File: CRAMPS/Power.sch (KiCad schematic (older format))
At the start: 19 parts, among them P101 HB_IN, P103 PS-ON, P105 12V-AUX, P107 MOT_IN, P108 POWER_IN, P219 EXT_5V, U3 LM7812

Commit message: Work in progress, many schematic updates, added PCB files
Signed-off-by: Charles Steinkuehler <charles@steinkuehler.net>
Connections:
- net labels added: D3.3V, SYS_5V, VDD_5V
- net labels removed: DUE_5V, FD_5V, IOREF
- wire segments 67 -> 83
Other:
- note added: "BeagleBone Logic supply is always 3.3V"
- note added: "SYS_5V: Low-current supply\nVDD_5V: DC Input Jack"
- note removed: "Note: On R3 compatible Arduinos, IOREF \nwill supply 3.3V (Due), or 5V (Mega).\n\nIf IOREF is not provided (non-R3) then it \nmust be a 5V Arduino so set VSEL to 5V."
- note removed: "VSEL - Select logic voltage\n1-2 = Autoselect by IOREF\n2-3 = 5V"
- moved on the sheet: JP101, JP201, P219

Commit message: Schematic updates mostly complete Pending pin assignment which will happen based on PCB layout Updated netlist imported to PCB, but placement not started
Signed-off-by: Charles Steinkuehler <charles@steinkuehler.net>
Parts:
- removed D103: ES1F, symbol DIODE
- removed JP1: VIN, symbol JUMPER
- removed JP101: VLOG, symbol JUMP_MINI_3
- removed JP201: 5V_SEL, ~, symbol JUMP_MINI
- removed P103: PS-ON, symbol CONN_1
- added P213: PS-ON, symbol CONN_2
- added P214: 5V_REG, symbol CONN_3X2
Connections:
- net labels added: +3.3V
- net labels removed: AM-VIN, LP_1
- wire segments 83 -> 70
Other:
- note added: "Provision for optional 5V regulator to allow stand-alone \noperation from POWER_IN\n\nA common 1A switching version of the 7805 will work to power the \nBeagleBone however verify input voltage specifications if POWER_IN\nis more than 12V. Also, more than 1A may be needed if there are\nhigh current drains on VDD_5V (typically servos or something\nconnected via the Aux. headers)"
- note added: "SYS_5V: Low-current supply"
- note added: "VDD_5V: DC Input Jack"
- note removed: "JP1: Supply 12V to Arduino in standalone operation\nRemove if Arduino is powered by USB or other supply"
- note removed: "SYS_5V: Low-current supply\nVDD_5V: DC Input Jack"
- moved on the sheet: P105, P219

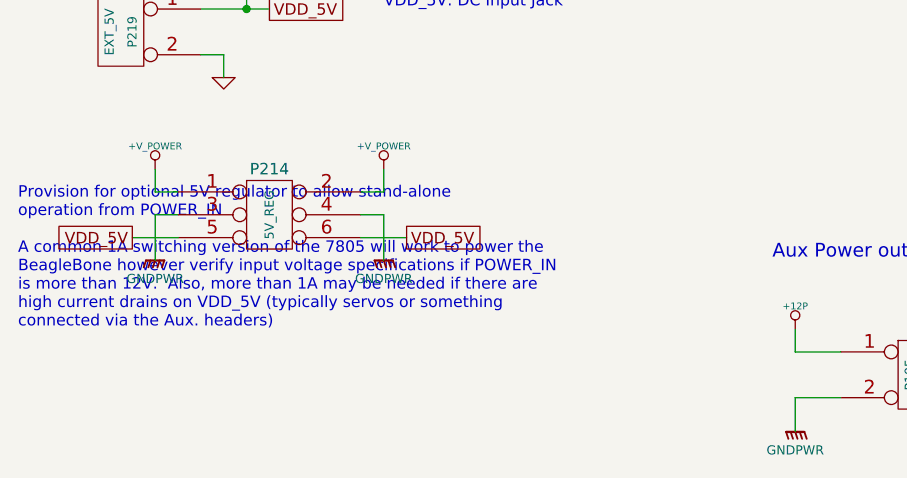
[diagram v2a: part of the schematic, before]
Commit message: P8/P9 Pins assigned, PCB placement in-progress
Signed-off-by: Charles Steinkuehler <charles@steinkuehler.net>
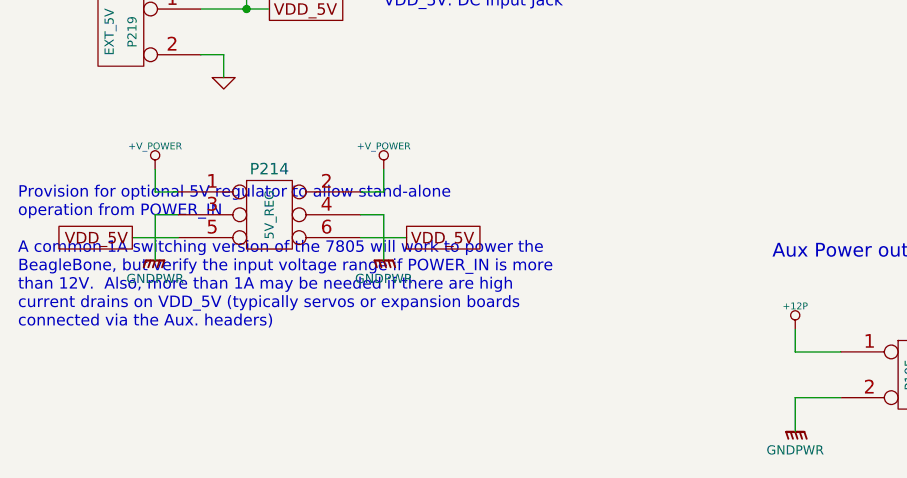
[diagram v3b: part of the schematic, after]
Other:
- note added: "Provision for optional 5V regulator to allow stand-alone \noperation from POWER_IN\n\nA common 1A switching version of the 7805 will work to power the \nBeagleBone, but verify the input voltage range if POWER_IN is more\nthan 12V. Also, more than 1A may be needed if there are high\ncurrent drains on VDD_5V (typically servos or expansion boards\nconnected via the Aux. headers)"
- note removed: "Provision for optional 5V regulator to allow stand-alone \noperation from POWER_IN\n\nA common 1A switching version of the 7805 will work to power the \nBeagleBone however verify input voltage specifications if POWER_IN\nis more than 12V. Also, more than 1A may be needed if there are\nhigh current drains on VDD_5V (typically servos or something\nconnected via the Aux. headers)"
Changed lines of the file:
@@
 Sheet 2 10
 Title "CRAMPS (Cape-RAMPS for BeagleBone)"
-Date "4 feb 2014"
+Date "6 feb 2014"
 Rev "v1.0"
 Comp ""
@@
 	1700 6600 1900 6600
 Text Notes 1200 7000 0    50   ~ 0
-Provision for optional 5V regulator to allow stand-alone \noperation from POWER_IN\n\nA common 1A switching version of the 7805 will work to power the \nBeagleBone however verify input voltage specifications if POWER_IN\nis more than 12V.  Also, more than 1A may be needed if there are\nhigh current drains on VDD_5V (typically servos or something\nconnected via the Aux. headers)
+Provision for optional 5V regulator to allow stand-alone \noperation from POWER_IN\n\nA common 1A switching version of the 7805 will work to power the \nBeagleBone, but verify the input voltage range if POWER_IN is more\nthan 12V.  Also, more than 1A may be needed if there are high\ncurrent drains on VDD_5V (typically servos or expansion boards\nconnected via the Aux. headers)
 $EndSCHEMATC

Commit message: Initial BOM files for PCB version 1.0 Added README and ToDo text files
Signed-off-by: Charles Steinkuehler <charles@steinkuehler.net>
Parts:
- C101: Mfg (none) -> Nichicon; PartNo (none) -> UCD1V101MCL6GS
- C102, C207: Mfg (none) -> Taiyo Yuden; PartNo (none) -> GMK212BJ104KGHT
- D102: Mfg (none) -> Vishay; PartNo (none) -> SS10P4-M3/86A
- F101, F102, F103: Mfg (none) -> Littlefuse; PartNo (none) -> 01530008Z
- JP102: Mfg (none) -> Harwin; PartNo (none) -> M20-9990345
- P101, P107, P108: Mfg (none) -> Phoenix; PartNo (none) -> 1715721
- P105: Mfg (none) -> Molex; PartNo (none) -> 22-23-2021
- P213: Mfg (none) -> Harwin; PartNo (none) -> M20-9990245
- P214: Mfg (none) -> Harwin; PartNo (none) -> M20-9980345
- P219: Mfg (none) -> Phoenix; PartNo (none) -> 1984617
- U3: Mfg (none) -> Fairchild; PartNo (none) -> LM7812ACT
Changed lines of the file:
@@
 Sheet 2 10
 Title "CRAMPS (Cape-RAMPS for BeagleBone)"
-Date "9 feb 2014"
+Date "11 feb 2014"
 Rev "v1.0"
 Comp ""
@@
 F 2 "" H 8300 5450 60  0001 C CNN
 F 3 "" H 8300 5450 60  0001 C CNN
+F 4 "Harwin" H 6250 6550 60  0001 C CNN "Mfg"
+F 5 "M20-9990345" H 6250 6550 60  0001 C CNN "PartNo"
 	1    8300 5450
 	1    0    0    -1
@@
 F 2 "" H 7250 5300 60  0001 C CNN
 F 3 "" H 7250 5300 60  0001 C CNN
+F 4 "Harwin" H 6250 6550 60  0001 C CNN "Mfg"
+F 5 "M20-9990345" H 6250 6550 60  0001 C CNN "PartNo"
 	1    7250 5300
 	1    0    0    -1
@@
 F 2 "" H 4750 3700 60  0001 C CNN
 F 3 "" H 4750 3700 60  0001 C CNN
+F 4 "Phoenix" H 6250 6550 60  0001 C CNN "Mfg"
+F 5 "1715721" H 6250 6550 60  0001 C CNN "PartNo"
 	1    4750 3700
 	-1   0    0    1
@@
 F 2 "" H 4750 1850 60  0001 C CNN
 F 3 "" H 4750 1850 60  0001 C CNN
+F 4 "Phoenix" H 6250 6550 60  0001 C CNN "Mfg"
+F 5 "1715721" H 6250 6550 60  0001 C CNN "PartNo"
 	1    4750 1850
 	-1   0    0    1
@@
 F 2 "" H 5850 2600 60  0001 C CNN
 F 3 "" H 5850 2600 60  0001 C CNN
+F 4 "Littlefuse" H 6250 6550 60  0001 C CNN "Mfg"
+F 5 "01530008Z" H 6250 6550 60  0001 C CNN "PartNo"
 	1    5850 2600
 	1    0    0    -1
@@
 F 2 "" H 4750 2700 60  0001 C CNN
 F 3 "" H 4750 2700 60  0001 C CNN
+F 4 "Phoenix" H 6250 6550 60  0001 C CNN "Mfg"
+F 5 "1715721" H 6250 6550 60  0001 C CNN "PartNo"
 	1    4750 2700
 	-1   0    0    1
@@
 F 2 "" H 5150 7200 60  0001 C CNN
 F 3 "" H 5150 7200 60  0001 C CNN
+F 4 "Molex" H 6250 6550 60  0001 C CNN "Mfg"
+F 5 "22-23-2021" H 6250 6550 60  0001 C CNN "PartNo"
 	1    5150 7200
 	1    0    0    -1
@@
 F 2 "" H 7500 3900 60  0001 C CNN
 F 3 "" H 7500 3900 60  0001 C CNN
+F 4 "Taiyo Yuden" H 6250 6550 60  0001 C CNN "Mfg"
+F 5 "GMK212BJ104KGHT" H 6250 6550 60  0001 C CNN "PartNo"
 	1    7500 3900
 	1    0    0    -1
@@
 F 2 "" H 6950 3900 60  0001 C CNN
 F 3 "" H 6950 3900 60  0001 C CNN
+F 4 "Nichicon" H 6950 3900 60  0001 C CNN "Mfg"
+F 5 "UCD1V101MCL6GS" H 6950 3900 60  0001 C CNN "PartNo"
 	1    6950 3900
 	1    0    0    -1
@@
 F 2 "" H 5850 3600 60  0001 C CNN
 F 3 "" H 5850 3600 60  0001 C CNN
+F 4 "Littlefuse" H 6250 6550 60  0001 C CNN "Mfg"
+F 5 "01530008Z" H 6250 6550 60  0001 C CNN "PartNo"
 	1    5850 3600
 	1    0    0    -1
@@
 F 2 "" H 5850 1750 60  0001 C CNN
 F 3 "" H 5850 1750 60  0001 C CNN
+F 4 "Littlefuse" H 6250 6550 60  0001 C CNN "Mfg"
+F 5 "01530008Z" H 6250 6550 60  0001 C CNN "PartNo"
 	1    5850 1750
 	1    0    0    -1
@@
 F 2 "~" H 6400 5350 60  0000 C CNN
 F 3 "~" H 6400 5350 60  0000 C CNN
+F 4 "Fairchild" H 6250 6550 60  0001 C CNN "Mfg"
+F 5 "LM7812ACT" H 6250 6550 60  0001 C CNN "PartNo"
 	1    6400 5350
 	1    0    0    -1
@@
 F 2 "" H 6900 5650 60  0001 C CNN
 F 3 "" H 6900 5650 60  0001 C CNN
+F 4 "Taiyo Yuden" H 6250 6550 60  0001 C CNN "Mfg"
+F 5 "GMK212BJ104KGHT" H 6250 6550 60  0001 C CNN "PartNo"
 	1    6900 5650
 	1    0    0    -1
@@
 F 2 "" H 1650 5700 60  0001 C CNN
 F 3 "" H 1650 5700 60  0001 C CNN
+F 4 "Phoenix" H 6250 6550 60  0001 C CNN "Mfg"
+F 5 "1984617" H 6250 6550 60  0001 C CNN "PartNo"
 	1    1650 5700
 	-1   0    0    -1
@@
 F 2 "" H 6500 3950 60  0000 C CNN
 F 3 "" H 6500 3950 60  0000 C CNN
-F 4 "If = 10 A" V 7000 3900 60  0000 C CNN "Note"
+F 4 "Vishay" H 6250 6550 60  0001 C CNN "Mfg"
+F 5 "SS10P4-M3/86A" H 6250 6550 60  0001 C CNN "PartNo"
+F 6 "If = 10 A" V 7000 3900 60  0000 C CNN "Note"
 	1    6500 3950
 	0    1    1    0
@@
 F 2 "" H 6650 7200 60  0001 C CNN
 F 3 "" H 6650 7200 60  0001 C CNN
+F 4 "Harwin" H 6250 6550 60  0001 C CNN "Mfg"
+F 5 "M20-9990245" H 6250 6550 60  0001 C CNN "PartNo"
 	1    6650 7200
 	1    0    0    -1
@@
 F 2 "" H 2300 6550 60  0001 C CNN
 F 3 "" H 2300 6550 60  0001 C CNN
+F 4 "Harwin" H 6250 6550 60  0001 C CNN "Mfg"
+F 5 "M20-9980345" H 6250 6550 60  0001 C CNN "PartNo"
 	1    2300 6550
 	1    0    0    -1

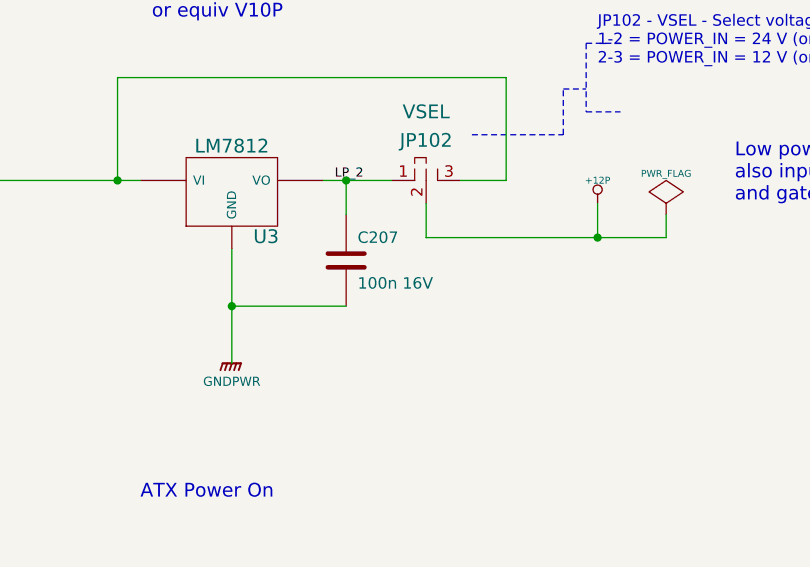
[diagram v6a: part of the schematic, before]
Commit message: BOM Updates Fixed incorrect Molex part number Added Stackpole resistor part numbers Switched to value-sorted BOM export from KiCAD Modified some attribute fields to get same-value parts to list on a single BOM line
Signed-off-by: Charles Steinkuehler <charles@steinkuehler.net>
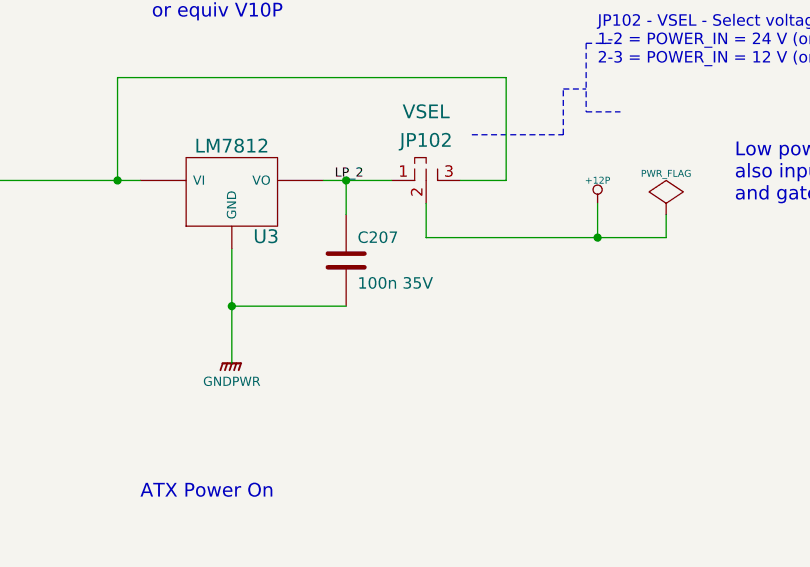
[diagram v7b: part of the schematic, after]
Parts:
- C207: value 100n 16V -> 100n 35V
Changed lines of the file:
@@
 Sheet 2 10
 Title "CRAMPS (Cape-RAMPS for BeagleBone)"
-Date "11 feb 2014"
+Date "15 feb 2014"
 Rev "v1.0"
 Comp ""
@@
 P 6900 5650
 F 0 "C207" H 6950 5750 50  0000 L CNN
-F 1 "100n 16V" H 6950 5550 50  0000 L CNN
+F 1 "100n 35V" H 6950 5550 50  0000 L CNN
 F 2 "" H 6900 5650 60  0001 C CNN
 F 3 "" H 6900 5650 60  0001 C CNN
